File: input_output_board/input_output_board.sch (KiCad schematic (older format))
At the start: 23 parts, among them J1 Neutrik_NCJ6FA-H, J2 Neutrik_NCJ6FA-H, J3 Neutrik_NCJ6FA-H, J4 Neutrik_NCJ6FA-H, J5 AudioJack3, J6 Conn_02x08_Odd_Even, J7 Molex_SL_01x04_Male, J8 Molex_SL_01x04_Male, K1 G6S-2, K2 G6S-2, K3 G6S-2, K4 G6S-2, K5 G6S-2

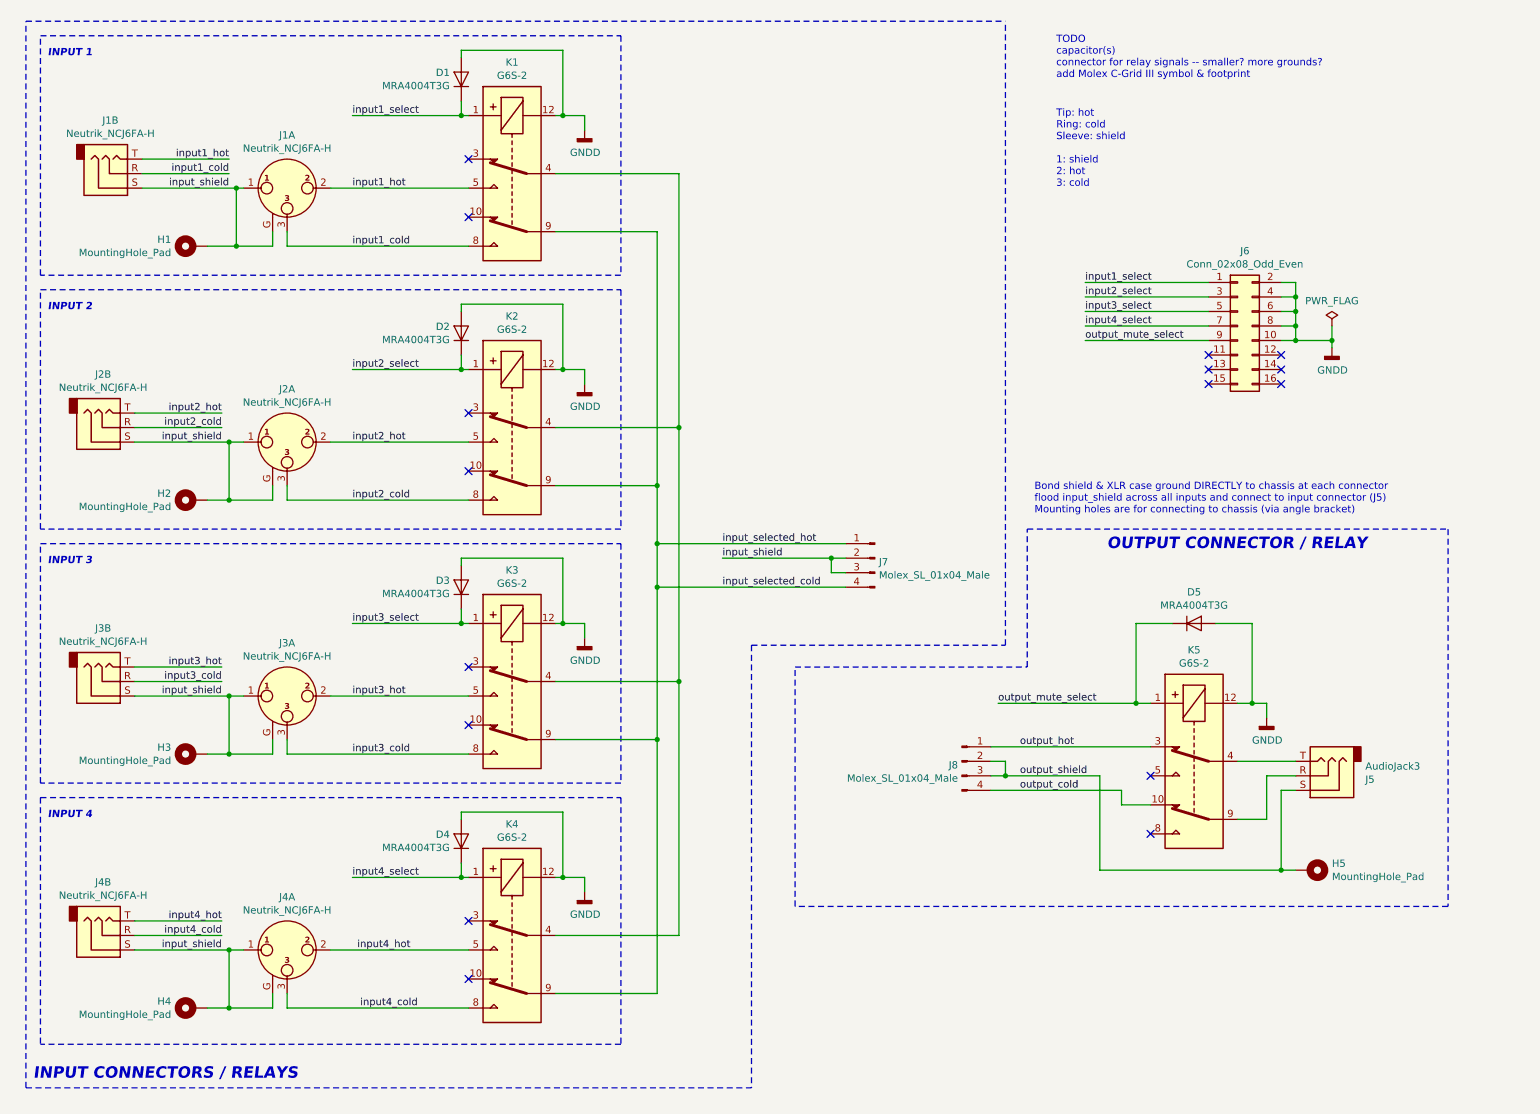
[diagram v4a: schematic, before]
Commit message: add part details to most connectors
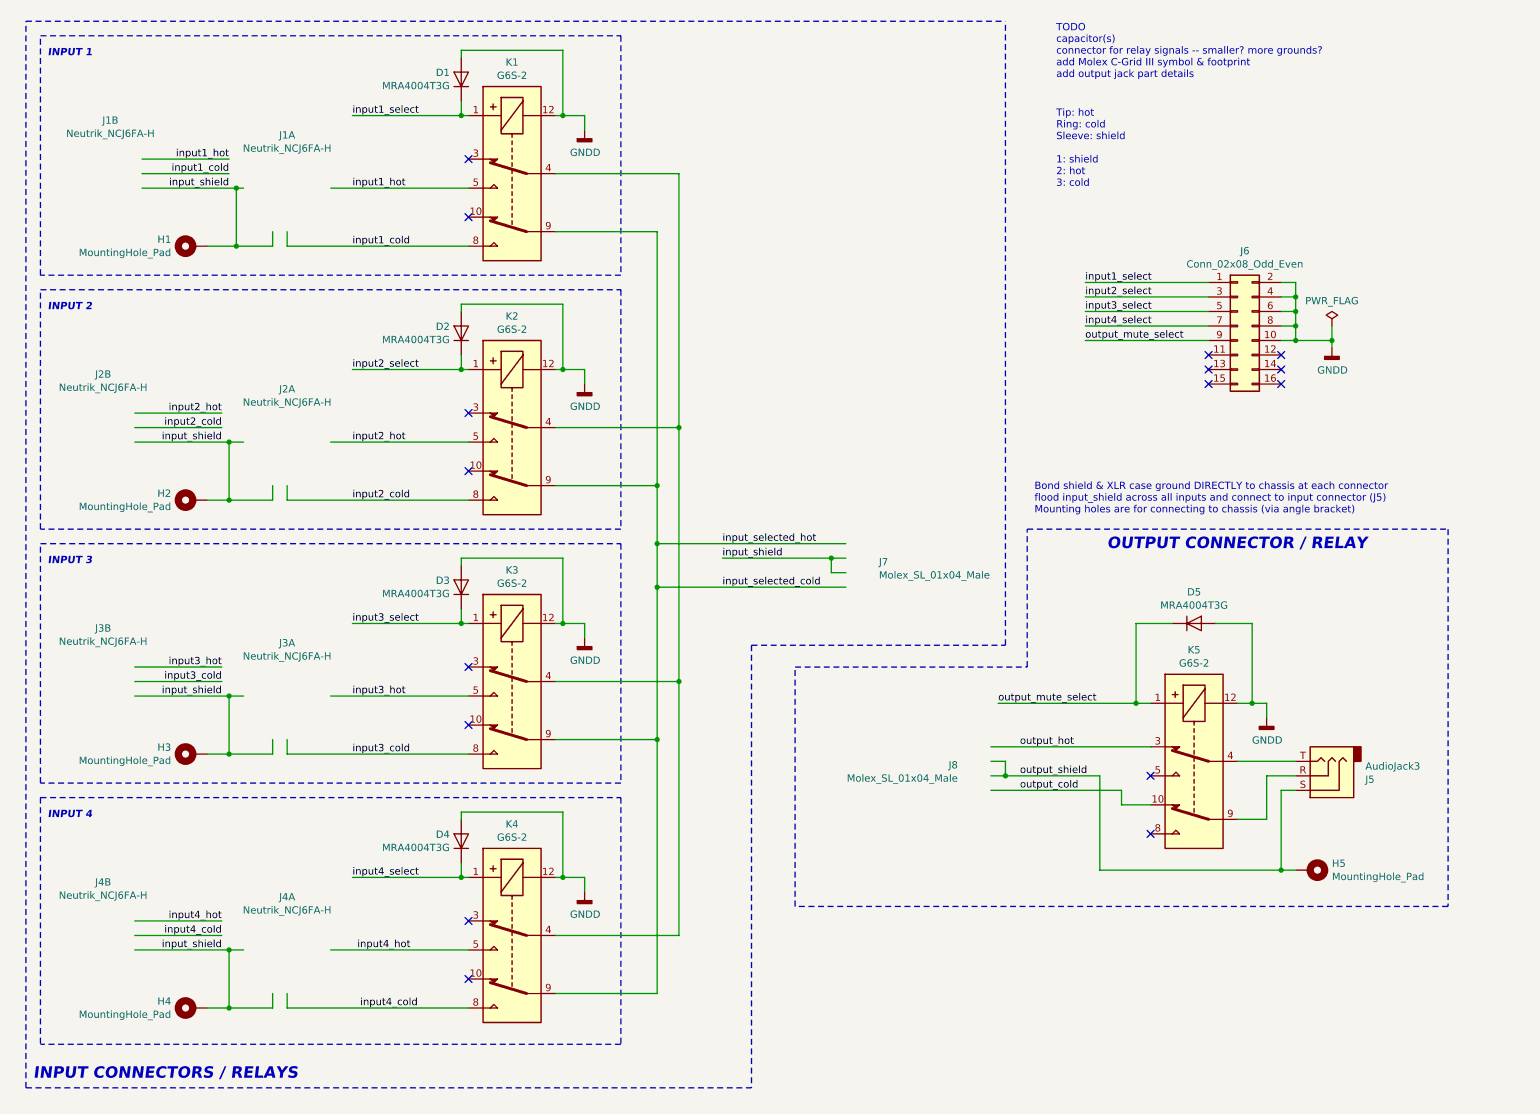
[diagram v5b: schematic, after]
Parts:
- removed J8: Molex_SL_01x04_Male, Connector_Molex_SL:Molex_SL_A-70543-0003_1x04_P2.54mm_Vertical, symbol Connector_gkeeth:Molex_SL_01x04_Male
- added J8: Molex_SL_01x04_Male, Connector_Molex_SL:Molex_SL_A-70543-0003_1x04_P2.54mm_Vertical, symbol Connector_gkeeth:Molex_SL_01x04_Male
- H1, H2, H3, H4, H5: footprint (none) -> MountingHole:MountingHole_3.2mm_M3_Pad_Via
- J1, J2, J3, J4: footprint (none) -> Connector_Audio_gkeeth:Jack_Combo_Neutrik_NCJ6FA-H_Horizontal; URL 2.10 -> https://www.mouser.com/ProductDetail/Neutrik/NCJ6FA-H?qs=aE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; Unit Price https://www.mouser.com/ProductDetail/Neutrik/NCJ6FA-H?qs=aE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 -> 2.10
- J1, J2, J3, J4: footprint (none) -> Connector_Audio_gkeeth:Jack_Combo_Neutrik_NCJ6FA-H_Horizontal; Distributor (none) -> Mouser; Distributor PN (none) -> 568-NCJ6FA-H; Manufacturer (none) -> Neutrik; Manufacturer PN (none) -> NCJ6FA-H; URL (none) -> https://www.mouser.com/ProductDetail/Neutrik/NCJ6FA-H?qs=aE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; Unit Price (none) -> 2.10
- J5: footprint (none) -> Connector_Audio:Jack_3.5mm_Neutrik_NMJ6HCD2_Horizontal
- J7: Distributor (none) -> Digikey; Distributor PN (none) -> WM4802-ND; Manufacturer (none) -> Molex; Manufacturer PN (none) -> 0705430003; URL (none) -> https://www.digikey.com/products/en?keywords=0705430003; Unit Price (none) -> 0.99
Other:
- note added: "TODO\ncapacitor(s)\nconnector for relay signals -- smaller? more grounds?\nadd Molex C-Grid III symbol & footprint\nadd output jack part details"
- note removed: "TODO\ncapacitor(s)\nconnector for relay signals -- smaller? more grounds?\nadd Molex C-Grid III symbol & footprint"
